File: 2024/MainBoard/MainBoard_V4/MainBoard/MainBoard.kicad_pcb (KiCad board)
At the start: 2 copper layers, 15 parts, among them J1 Raspberry_Pi_2_3, SW1 SW_MEC_5E, U1 STM32F446RETx, Y1 CSTNE16M0V530000R0

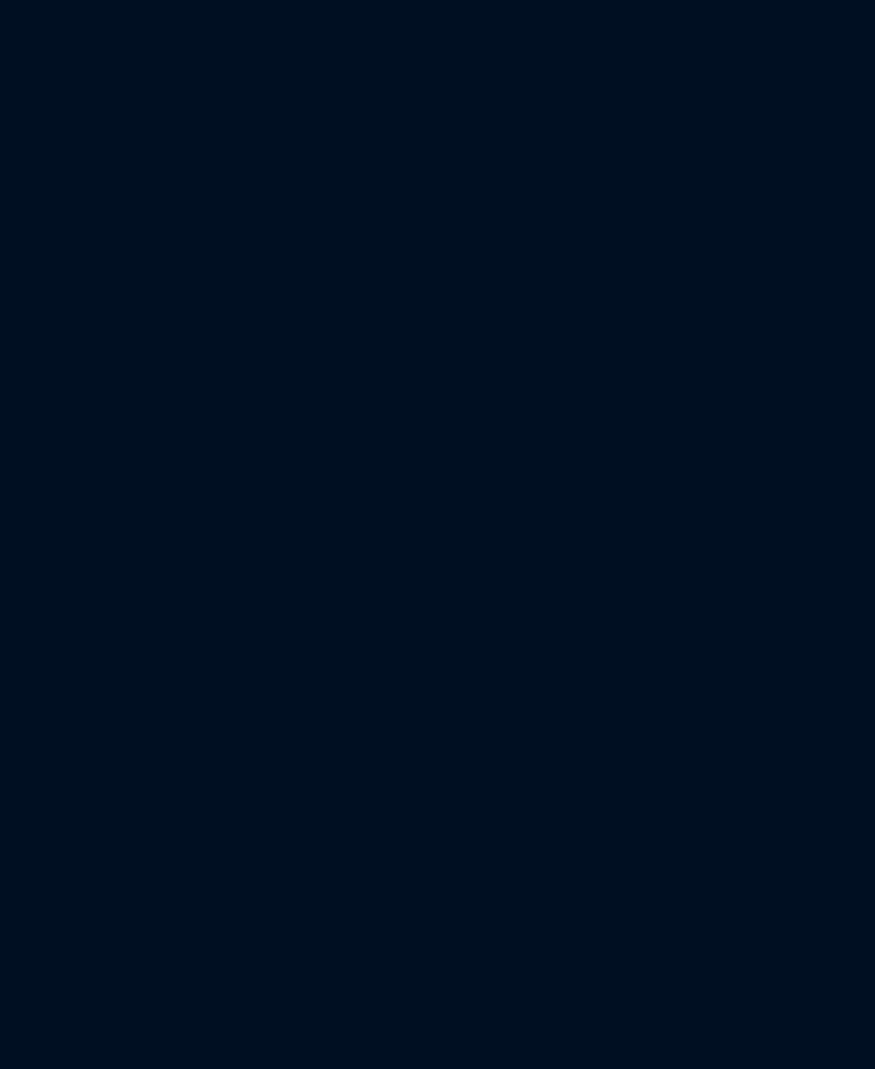
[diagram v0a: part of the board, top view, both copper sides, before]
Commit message: ✨ラズパイ周りとUSBシリアル変換周りの回路図を描いた
 USBを刺した時にラズパイが5Vで起動しないようにしないといけない?
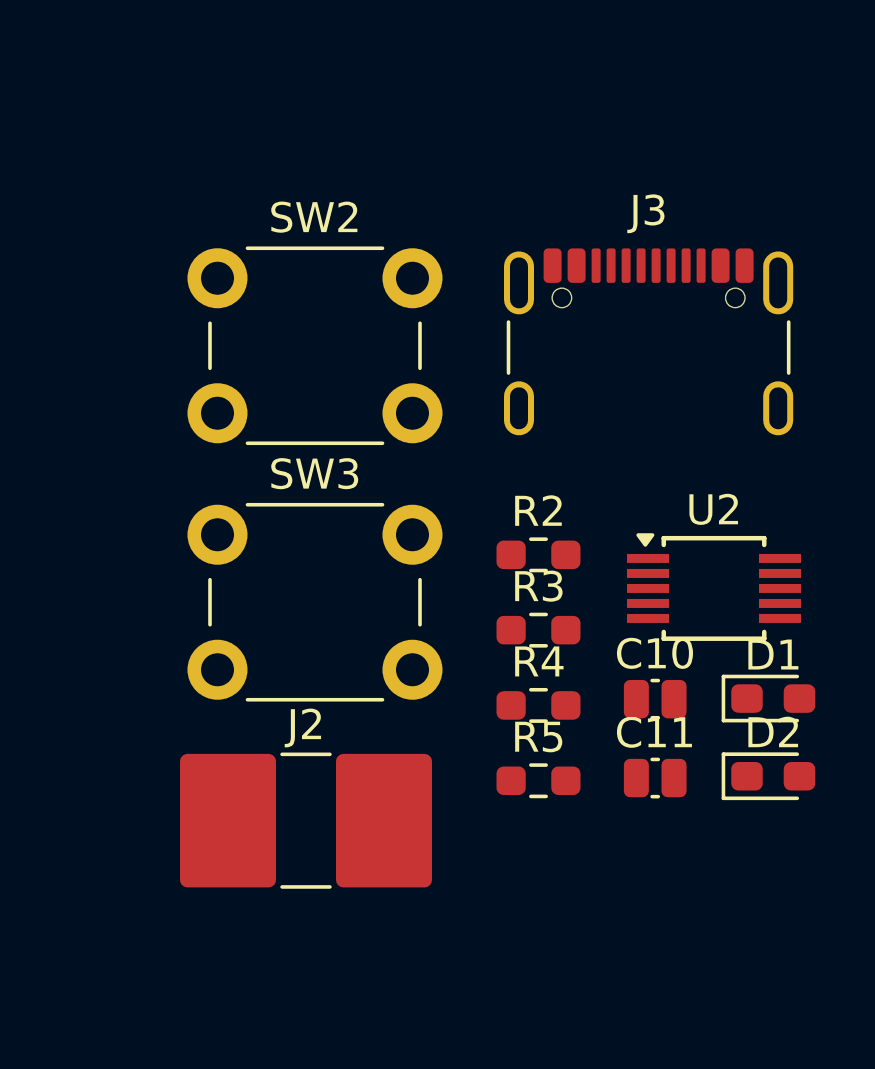
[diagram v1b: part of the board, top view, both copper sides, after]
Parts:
- added C10: 0.1u, Capacitor_SMD:C_0504_1310Metric_Pad0.83x1.28mm_HandSolder, F.Cu at (129.1, 53.7)
- added C11: 0.1u, Capacitor_SMD:C_0504_1310Metric_Pad0.83x1.28mm_HandSolder, F.Cu at (129.1, 56.3)
- added D1: LED, LED_SMD:LED_0603_1608Metric_Pad1.05x0.95mm_HandSolder, F.Cu at (133.0, 53.7)
- added D2: LED, LED_SMD:LED_0603_1608Metric_Pad1.05x0.95mm_HandSolder, F.Cu at (133.0, 56.3)
- added J2: fan, Resistor_SMD:R_2816_7142Metric_Pad3.20x4.45mm_HandSolder, F.Cu at (117.5, 57.8)
- added J3: USB_C_Receptacle_USB2.0_16P, Connector_USB:USB_C_Receptacle_GCT_USB4105-xx-A_16P_TopMnt_Horizontal, F.Cu at (128.9, 42.9)
- added R2: 470, Resistor_SMD:R_0603_1608Metric_Pad0.98x0.95mm_HandSolder, F.Cu at (125.2, 48.9)
- added R3: 5.1k, Resistor_SMD:R_0603_1608Metric_Pad0.98x0.95mm_HandSolder, F.Cu at (125.2, 51.4)
- added R4: 5.1k, Resistor_SMD:R_0603_1608Metric_Pad0.98x0.95mm_HandSolder, F.Cu at (125.2, 53.9)
- added R5: 470, Resistor_SMD:R_0603_1608Metric_Pad0.98x0.95mm_HandSolder, F.Cu at (125.2, 56.4)
- added SW2: SW_MEC_5E, Button_Switch_THT:SW_PUSH_6mm, F.Cu at (114.5, 39.7)
- added SW3: SW_MEC_5E, Button_Switch_THT:SW_PUSH_6mm, F.Cu at (114.5, 48.2)
- added U2: CH340E, Package_SO:MSOP-10_3x3mm_P0.5mm, F.Cu at (131.1, 50.0)
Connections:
- net Net-(J1-5V-Pad2) renamed +5V
- net UART5_TX renamed Ras_RX
- net USB_RX renamed UART2_RX
- net USB_TX renamed UART2_TX
- J1 pad 1: Net-(J1-3V3-Pad1) -> unconnected-(J1-3V3-Pad1)
- J1 pad 10: unconnected-(J1-GPIO15/RXD-Pad10) -> Ras_TX
- J1 pad 12: unconnected-(J1-GPIO18/PWM0-Pad12) -> LED_RAS1
- J1 pad 13: unconnected-(J1-GPIO27-Pad13) -> LED_RAS2
- J1 pad 14: Net-(J1-GND-Pad14) -> GND
- J1 pad 15: unconnected-(J1-GPIO22-Pad15) -> SW_RAS2
- J1 pad 17: Net-(J1-3V3-Pad1) -> unconnected-(J1-3V3-Pad1)
- J1 pad 18: unconnected-(J1-GPIO24-Pad18) -> SW_RAS1
- J1 pad 20: Net-(J1-GND-Pad14) -> GND
- J1 pad 22: unconnected-(J1-GPIO25-Pad22) -> R4
- J1 pad 25: Net-(J1-GND-Pad14) -> GND
- J1 pad 29: unconnected-(J1-GCLK1/GPIO5-Pad29) -> R2
- J1 pad 30: Net-(J1-GND-Pad14) -> GND
- J1 pad 31: unconnected-(J1-GCLK2/GPIO6-Pad31) -> R3
- J1 pad 33: unconnected-(J1-PWM1/GPIO13-Pad33) -> RAS_AUDIO
- J1 pad 34: Net-(J1-GND-Pad14) -> GND
- J1 pad 39: Net-(J1-GND-Pad14) -> GND
- J1 pad 6: Net-(J1-GND-Pad14) -> GND
- J1 pad 7: unconnected-(J1-GCLK0/GPIO4-Pad7) -> R1
- J1 pad 8: unconnected-(J1-GPIO14/TXD-Pad8) -> Ras_TX
- J1 pad 9: Net-(J1-GND-Pad14) -> GND
- U1 pad 42: unconnected-(U1-PA9-Pad42) -> SER_RX
- U1 pad 43: unconnected-(U1-PA10-Pad43) -> SER_TX
- U1 pad 54: UART5_RX -> Ras_TX

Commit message: ✨DXFをインポートした
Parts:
- removed JP1: Jumper_2_Open, Connector_PinHeader_2.54mm:PinHeader_1x02_P2.54mm_Vertical
- added C12: 0.1u, Capacitor_SMD:C_0603_1608Metric_Pad1.08x0.95mm_HandSolder, F.Cu at (82.9, 7.79)
- added C13: 0.1u, Capacitor_SMD:C_0603_1608Metric_Pad1.08x0.95mm_HandSolder, F.Cu at (82.9, 10.3)
- added C14: 1u, Capacitor_SMD:C_0603_1608Metric_Pad1.08x0.95mm_HandSolder, F.Cu at (82.9, 12.8)
- added C15: 1u, Capacitor_SMD:C_0603_1608Metric_Pad1.08x0.95mm_HandSolder, F.Cu at (82.9, 15.3)
- added C16: 0.1u, Capacitor_SMD:C_0603_1608Metric_Pad1.08x0.95mm_HandSolder, F.Cu at (82.9, 17.8)
- added C17: 0.1u, Capacitor_SMD:C_0603_1608Metric_Pad1.08x0.95mm_HandSolder, F.Cu at (82.9, 20.3)
- added C18: 0.1u, Capacitor_SMD:C_0603_1608Metric_Pad1.08x0.95mm_HandSolder, F.Cu at (82.9, 22.8)
- added D10: LED, LED_SMD:LED_0603_1608Metric_Pad1.05x0.95mm_HandSolder, F.Cu at (100.4, 18.2)
- added D11: LED, LED_SMD:LED_0603_1608Metric_Pad1.05x0.95mm_HandSolder, F.Cu at (100.4, 20.8)
- added D12: LED, LED_SMD:LED_0603_1608Metric_Pad1.05x0.95mm_HandSolder, F.Cu at (100.4, 23.4)
- added D13: LED, LED_SMD:LED_0603_1608Metric_Pad1.05x0.95mm_HandSolder, F.Cu at (100.4, 26.0)
- added D14: LED, LED_SMD:LED_0603_1608Metric_Pad1.05x0.95mm_HandSolder, F.Cu at (100.4, 28.5)
- added D15: LED, LED_SMD:LED_0603_1608Metric_Pad1.05x0.95mm_HandSolder, F.Cu at (100.4, 31.1)
- added D3: LED, LED_SMD:LED_0603_1608Metric_Pad1.05x0.95mm_HandSolder, F.Cu at (100.4, 7.83)
- added D4: 1N4148W, Diode_SMD:D_SOD-123, F.Cu at (128.4, 8.21)
- added D5: 1N4148, Diode_THT:D_DO-35_SOD27_P7.62mm_Horizontal, F.Cu at (87.0, 39.4)
- added D6: 1N4148W, Diode_SMD:D_SOD-123, F.Cu at (128.4, 11.6)
- added D7: LED, LED_SMD:LED_0603_1608Metric_Pad1.05x0.95mm_HandSolder, F.Cu at (100.4, 10.4)
- added D8: LED, LED_SMD:LED_0603_1608Metric_Pad1.05x0.95mm_HandSolder, F.Cu at (100.4, 13.0)
- added D9: LED, LED_SMD:LED_0603_1608Metric_Pad1.05x0.95mm_HandSolder, F.Cu at (100.4, 15.6)
- added H1: MountingHole_Pad, MountingHole:MountingHole_3.2mm_M3_Pad_Via, F.Cu at (7.70, -24.2)
- added H2: MountingHole_Pad, MountingHole:MountingHole_3.2mm_M3_Pad_Via, F.Cu at (-50.3, -24.2)
- added H3: MountingHole_Pad, MountingHole:MountingHole_3.2mm_M3_Pad_Via, F.Cu at (44.5, -24.2)
- added H4: MountingHole_Pad, MountingHole:MountingHole_3.2mm_M3_Pad_Via, F.Cu at (-50.3, 24.8)
- added H5: MountingHole_Pad, MountingHole:MountingHole_3.2mm_M3_Pad_Via, F.Cu at (7.70, 24.8)
- added H6: MountingHole_Pad, MountingHole:MountingHole_3.2mm_M3_Pad_Via, F.Cu at (44.5, 24.8)
- added J10: ADC3, Connector_JST:JST_XH_S3B-XH-A_1x03_P2.50mm_Horizontal, F.Cu at (100.2, -3.69)
- added J11: ADC2, Connector_JST:JST_XH_S3B-XH-A_1x03_P2.50mm_Horizontal, F.Cu at (112.1, -3.69)
- added J12: ADC2, Connector_JST:JST_XH_S3B-XH-A_1x03_P2.50mm_Horizontal, F.Cu at (124.1, -3.69)
- added J13: Drib, Connector_JST:JST_XH_S2B-XH-A_1x02_P2.50mm_Horizontal, F.Cu at (88.9, 27.4)
- added J14: UART, Connector_JST:JST_XH_S4B-XH-A_1x04_P2.50mm_Horizontal, F.Cu at (106.0, 9.86)
- added J15: TFT3, Connector_PinHeader_2.54mm:PinHeader_1x04_P2.54mm_Vertical, F.Cu at (125.4, 29.4)
- added J16: CAN_CON, Connector_JST:JST_PH_S2B-PH-K_1x02_P2.00mm_Horizontal, F.Cu at (118.1, 29.4)
- added J4: CAN_CON, Connector_JST:JST_PH_S2B-PH-K_1x02_P2.00mm_Horizontal, F.Cu at (110.2, 29.4)
- added J5: MOLEX MINISPOX, Connector_Molex:Molex_SPOX_5267-06A_1x06_P2.50mm_Vertical, F.Cu at (110.7, 24.2)
- added J6: Debug, Connector_PinHeader_2.54mm:PinHeader_1x07_P2.54mm_Vertical, F.Cu at (83.1, 26.4)
- added J7: ADC0, Connector_JST:JST_XH_S3B-XH-A_1x03_P2.50mm_Horizontal, F.Cu at (64.3, -3.69)
- added J8: ADC1, Connector_JST:JST_XH_S3B-XH-A_1x03_P2.50mm_Horizontal, F.Cu at (76.3, -3.69)
- added J9: ADC2, Connector_JST:JST_XH_S3B-XH-A_1x03_P2.50mm_Horizontal, F.Cu at (88.2, -3.69)
- added Q1: NMOS, MainBoard:SOT95P240X111-3N, F.Cu at (128.4, 15.5)
- added R10: 4.7k, Resistor_SMD:R_0603_1608Metric_Pad0.98x0.95mm_HandSolder, F.Cu at (87.3, 17.8)
- added R11: 1k, Resistor_SMD:R_0603_1608Metric_Pad0.98x0.95mm_HandSolder, F.Cu at (87.3, 20.3)
- added R12: 1k, Resistor_SMD:R_0603_1608Metric_Pad0.98x0.95mm_HandSolder, F.Cu at (87.3, 22.8)
- added R13: 1k, Resistor_SMD:R_0603_1608Metric_Pad0.98x0.95mm_HandSolder, F.Cu at (91.6, 7.79)
- added R14: 1k, Resistor_SMD:R_0603_1608Metric_Pad0.98x0.95mm_HandSolder, F.Cu at (91.6, 10.3)
- added R15: 1k, Resistor_SMD:R_0603_1608Metric_Pad0.98x0.95mm_HandSolder, F.Cu at (91.6, 12.8)
- added R16: 1k, Resistor_SMD:R_0603_1608Metric_Pad0.98x0.95mm_HandSolder, F.Cu at (91.6, 15.3)
- added R17: 1k, Resistor_SMD:R_0603_1608Metric_Pad0.98x0.95mm_HandSolder, F.Cu at (91.6, 17.8)
- added R18: 1k, Resistor_SMD:R_0603_1608Metric_Pad0.98x0.95mm_HandSolder, F.Cu at (91.6, 20.3)
- added R19: 1k, Resistor_SMD:R_0603_1608Metric_Pad0.98x0.95mm_HandSolder, F.Cu at (91.6, 22.8)
- added R20: 120, Resistor_SMD:R_0603_1608Metric_Pad0.98x0.95mm_HandSolder, F.Cu at (96.0, 7.79)
- added R21: 1k, Resistor_SMD:R_0603_1608Metric_Pad0.98x0.95mm_HandSolder, F.Cu at (96.0, 10.3)
- added R22: 1k, Resistor_SMD:R_0603_1608Metric_Pad0.98x0.95mm_HandSolder, F.Cu at (96.0, 12.8)
- added R23: 10K, Resistor_SMD:R_0603_1608Metric_Pad0.98x0.95mm_HandSolder, F.Cu at (96.0, 15.3)
- added R6: 1k, Resistor_SMD:R_0603_1608Metric_Pad0.98x0.95mm_HandSolder, F.Cu at (87.3, 7.79)
- added R7: 1k, Resistor_SMD:R_0603_1608Metric_Pad0.98x0.95mm_HandSolder, F.Cu at (87.3, 10.3)
- added R8: 2.2k, Resistor_SMD:R_0603_1608Metric_Pad0.98x0.95mm_HandSolder, F.Cu at (87.3, 12.8)
- added R9: 2.2k, Resistor_SMD:R_0603_1608Metric_Pad0.98x0.95mm_HandSolder, F.Cu at (87.3, 15.3)
- added SW4: SW_Wuerth_450301014042, Button_Switch_THT:SW_Slide-03_Wuerth-WS-SLTV_10x2.5x6.4_P2.54mm, F.Cu at (71.3, 39.2)
- added U3: MOUDLE-SEEEDUINO-XIAO, MainBoard:MOUDLE14P-SMD-2.54-21X17.8MM, F.Cu at (61.9, 28.1)
- added U4: ~, Connector_PinHeader_2.54mm:PinHeader_1x08_P2.54mm_Vertical, F.Cu at (104.9, 22.4)
- added U5: ~, Connector_PinHeader_2.54mm:PinHeader_1x05_P2.54mm_Vertical, F.Cu at (63.2, 31.2)
- added U6: ~, Connector_PinHeader_2.54mm:PinHeader_1x04_P2.54mm_Vertical, F.Cu at (-3.81, -3.80)
- added U7: AZ1117-3.3, Package_TO_SOT_SMD:SOT-223-3_TabPin2, F.Cu at (70.4, 33.0)
- added U8: MAX3051, Package_SO:SOIC-8_3.9x4.9mm_P1.27mm, F.Cu at (121.2, 9.89)
- C1, C10, C11, C2, C3, C4, C5, C6, C7, C9: footprint Capacitor_SMD:C_0504_1310Metric_Pad0.83x1.28mm_HandSolder -> Capacitor_SMD:C_0603_1608Metric_Pad1.08x0.95mm_HandSolder
- C8: value 0.1u -> 4.7u; footprint Capacitor_SMD:C_0504_1310Metric_Pad0.83x1.28mm_HandSolder -> Capacitor_SMD:C_0603_1608Metric_Pad1.08x0.95mm_HandSolder
- R1: value R -> 10k
- R2: value 470 -> 1k
- moved SW1 148.2 mm to (137.3, -31.0)
- moved C1 148.2 mm to (120.5, -32.1)
- moved C2 148.2 mm to (120.5, -29.4)
- moved C3 148.2 mm to (120.5, -26.8)
- moved C4 148.2 mm to (123.9, -32.1)
- moved C5 148.2 mm to (123.9, -29.4)
- moved C6 148.2 mm to (123.9, -26.8)
- moved C7 148.2 mm to (127.3, -32.1)
- moved C8 148.2 mm to (127.3, -29.4)
- moved C9 148.2 mm to (127.3, -26.8)
- moved R1 148.2 mm to (135.9, -23.9)
- moved U1 148.2 mm to (111.5, -26.2)
- moved Y1 148.2 mm to (136.6, -26.9)
- moved C11 87.1 mm to (86.4, -19.6)
- moved D1 87.1 mm to (90.3, -22.2)
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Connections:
- net Net-(SW1-A) renamed NRST
- net SER_RX renamed UART1_TX
- net SER_TX renamed UART1_RX
- C11 pad 1: +5V -> +5VL
- J3 pad A4: Net-(J3-VBUS-PadA4) -> +5VL
- J3 pad A9: Net-(J3-VBUS-PadA4) -> +5VL
- J3 pad B4: Net-(J3-VBUS-PadA4) -> +5VL
- J3 pad B9: Net-(J3-VBUS-PadA4) -> +5VL
- R2 pad 2: Net-(J3-VBUS-PadA4) -> +5VL
- U1 pad 16: UART2_TX -> Port_RX
- U1 pad 17: UART2_RX -> Port_TX
- U2 pad 10: unconnected-(U2-V3-Pad10) -> Net-(U2-V3)
- U2 pad 7: unconnected-(U2-VCC-Pad7) -> +5VL
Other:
- board outline added: 115.8 x 60 mm

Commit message: 部品をおいた
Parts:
- removed J4: CAN_CON, Connector_JST:JST_PH_S2B-PH-K_1x02_P2.00mm_Horizontal
- added LS1: PKLCS1212E4001-R1, MainBoard:SPKR_PKLCS1212E4001-R1, F.Cu at (27.9, 20.3)
- added ROTSW1: SW_Coded_SH-7070, Button_Switch_THT:Nidec_Copal_SH-7010C, F.Cu at (-60.8, 10.5)
- J10, J11, J12, J7, J8, J9: footprint Connector_JST:JST_XH_S3B-XH-A_1x03_P2.50mm_Horizontal -> Connector_JST:JST_PH_B3B-PH-K_1x03_P2.00mm_Vertical
- J13, J14, J16, J2: moved to B.Cu
- U5: footprint Connector_PinHeader_2.54mm:PinHeader_1x05_P2.54mm_Vertical -> Connector_PinHeader_2.54mm:PinHeader_1x04_P2.54mm_Vertical
- moved J12 186.5 mm to (-60.5, 23.2)
- moved J11 173.6 mm to (-60.4, 16.0)
- moved U4 155.2 mm to (-45.7, -15.2)
- moved J16 151.0 mm to (-32.7, 21.6), turned to 180 degrees
- moved J13 129.1 mm to (-39.9, 18.5), turned to 180 degrees
- moved SW3 129.1 mm to (-55.6, -6.88), turned to -90 degrees
- moved SW2 129.0 mm to (-55.9, -17.8), turned to -90 degrees
- moved J14 125.3 mm to (-19.0, 18.4), turned to 180 degrees
- moved J5 123.2 mm to (-12.5, 25.4)
- moved U8 121.3 mm to (0.00, 12.7)
- moved U5 111.4 mm to (-45.7, 7.62)
- moved J6 106.8 mm to (-22.9, 12.7), turned to 90 degrees
- moved U1 98.4 mm to (17.2, 1.83)
- moved SW1 96.0 mm to (48.3, 5.08), turned to 90 degrees
- moved J15 95.4 mm to (35.6, -2.54)
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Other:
- board size 115.8 x 60 mm -> 115.8 x 60.5 mm

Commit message: わくぎめ
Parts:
- added J4: CAN_CON, Connector_JST:JST_PH_S2B-PH-K_1x02_P2.00mm_Horizontal, F.Cu at (76.3, -6.51)
- J10, J8, J9: footprint Connector_JST:JST_PH_B3B-PH-K_1x03_P2.00mm_Vertical -> Connector_JST:JST_PH_S3B-PH-K_1x03_P2.00mm_Horizontal
- J11, J12, J7: footprint Connector_JST:JST_PH_B3B-PH-K_1x03_P2.00mm_Vertical -> Connector_JST:JST_PH_S3B-PH-K_1x03_P2.00mm_Horizontal; moved to B.Cu
- J5: footprint Connector_Molex:Molex_SPOX_5267-06A_1x06_P2.50mm_Vertical -> Connector_Molex:Molex_SPOX_5268-06A_1x06_P2.50mm_Horizontal; moved to B.Cu
- SW2, SW3: footprint Button_Switch_THT:SW_PUSH_6mm -> MainBoard:SW_SKRPACE010
- moved J7 137.7 mm to (-55.8, 24.6), turned to 90 degrees
- moved C1 64.4 mm to (58.1, -16.2)
- moved C2 64.4 mm to (58.1, -13.6)
- moved C3 64.4 mm to (58.1, -10.9)
- moved C4 64.4 mm to (61.5, -16.2)
- moved C5 64.4 mm to (61.5, -13.6)
- moved C6 64.4 mm to (61.5, -10.9)
- moved C7 64.4 mm to (64.9, -16.2)
- moved C8 64.4 mm to (64.9, -13.6)
- moved C9 64.4 mm to (64.9, -10.9)
- moved U7 57.2 mm to (15.6, 16.5)
- moved SW2 27.4 mm to (-60.4, 9.23)
- moved J16 15.9 mm to (-16.8, 21.3)
- moved J5 14.4 mm to (1.23, 21.1), turned to 180 degrees
- moved ROTSW1 12.5 mm to (-61.0, -1.95)
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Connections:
- J1 pad 10: Ras_TX -> Ras_RX

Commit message: 途中経過
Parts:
- added Q2: PMOS, Package_TO_SOT_SMD:SOT-23, F.Cu at (14.3, 22.0)
- added Q3: PMOS, Package_TO_SOT_SMD:SOT-23, F.Cu at (18.5, 22.0)
- D5: footprint Diode_THT:D_DO-35_SOD27_P7.62mm_Horizontal -> Diode_SMD:D_SOD-123
- moved C10 134.8 mm to (-48.1, -30.2)
- moved D6 128.4 mm to (0.76, 26.2), turned to 180 degrees
- moved Y1 126.5 mm to (13.2, 0.91), turned to -90 degrees
- moved Q1 98.6 mm to (30.4, 26.3)
- moved R10 94.5 mm to (-6.84, 26.2)
- moved R11 90.9 mm to (-3.41, 26.2)
- moved R9 86.4 mm to (2.54, -1.52)
- moved R8 86.2 mm to (2.54, -3.17)
- moved D15 86.1 mm to (130.5, -49.5)
- moved R22 83.0 mm to (14.1, 26.3), turned to 180 degrees
- moved R23 76.4 mm to (20.3, 26.2), turned to 180 degrees
- moved D10 72.1 mm to (113.6, -52.7)
- moved D11 72.1 mm to (113.6, -50.1)
- moved D12 72.1 mm to (113.6, -47.5)
- moved D13 72.1 mm to (113.6, -44.9)
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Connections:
- J16 pad 1: CANH -> CANL
- J16 pad 2: CANL -> CANH
- J6 pad 1: UART_RX -> UART1_TX
- J6 pad 2: UART_TX -> UART1_RX
- J6 pad 6: VDD -> +3.3V
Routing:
- net GND: track 0.00 -> 243.3 mm, vias 0 -> 3
- net +3.3V: track 0.00 -> 237.3 mm
- net +5V: track 0.00 -> 160.2 mm, vias 0 -> 1
- net MOSI: track 0.00 -> 114.4 mm, vias 0 -> 2
- net MISO: track 0.00 -> 109.9 mm, vias 0 -> 2
- net SCK: track 0.00 -> 108.8 mm, vias 0 -> 2
- net LED_CS: track 0.00 -> 104.0 mm
- net T_CS: track 0.00 -> 85.8 mm
- net Ras_TX: track 0.00 -> 84.4 mm, vias 0 -> 1
- net LCD_LED: track 0.00 -> 81.8 mm, vias 0 -> 1
- net Ras_RX: track 0.00 -> 81.8 mm, vias 0 -> 1
- net D/C: track 0.00 -> 79.5 mm
- net Reset: track 0.00 -> 78.4 mm
- net +5VL: track 0.00 -> 64.2 mm, vias 0 -> 4
- net SWCLK: track 0.00 -> 54.3 mm, vias 0 -> 2
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
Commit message: 8割完成
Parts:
- removed J10: ADC3, Connector_JST:JST_PH_S3B-PH-K_1x03_P2.00mm_Horizontal
- removed J4: CAN_CON, Connector_JST:JST_PH_S2B-PH-K_1x02_P2.00mm_Horizontal
- removed J8: ADC1, Connector_JST:JST_PH_S3B-PH-K_1x03_P2.00mm_Horizontal
- removed J9: ADC2, Connector_JST:JST_PH_S3B-PH-K_1x03_P2.00mm_Horizontal
- R8, R9: moved to B.Cu
- moved R1 99.4 mm to (39.7, 1.40), turned to 90 degrees
- moved R20 92.5 mm to (-5.40, 16.4), turned to 180 degrees
- moved C16 76.7 mm to (6.30, 15.6), turned to -90 degrees
- moved D4 57.5 mm to (75.2, 30.2)
- moved D6 24.4 mm to (8.40, 3.00), turned to -90 degrees
- moved R11 22.4 mm to (8.40, 7.17), turned to 90 degrees
- moved R5 22.0 mm to (84.4, -41.5)
- moved D2 22.0 mm to (92.2, -41.6)
- moved D1 22.0 mm to (92.2, -44.2)
- moved R2 22.0 mm to (84.4, -49.0)
- moved R10 21.8 mm to (8.40, 10.6), turned to 90 degrees
- moved C9 19.4 mm to (49.8, 1.20), turned to 180 degrees
- moved C8 18.5 mm to (11.7, 11.2)
- moved D5 17.7 mm to (75.0, 26.4)
- moved C5 17.5 mm to (14.1, -2.96), turned to -90 degrees
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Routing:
- net GND: track 243.3 -> 443.7 mm, vias 3 -> 8
- net NRST: track 0.00 -> 93.7 mm, vias 0 -> 3
- net ADC_PHOTO1: track 0.00 -> 93.2 mm, vias 0 -> 4
- net ADC_SUB0: track 0.00 -> 89.5 mm, vias 0 -> 3
- net ADC_PHOTO0: track 0.00 -> 84.2 mm, vias 0 -> 3
- net +5V: track 160.2 -> 234.5 mm, vias 1 -> 3
- net DRIB_OUT: track 0.00 -> 72.7 mm, vias 0 -> 3
- net Port_RX: track 0.00 -> 65.9 mm, vias 0 -> 2
- net +3.3V: track 237.3 -> 302.7 mm
- net Port_TX: track 0.00 -> 63.7 mm, vias 0 -> 2
- net UART1_TX: track 25.6 -> 85.7 mm, vias 2 -> 4
- net UART1_RX: track 26.3 -> 81.2 mm, vias 2 -> 3
- net I2C_SDA: track 23.1 -> 30.5 mm, vias 1 -> 4
- net SWDIO: track 50.3 -> 57.7 mm
- net UART4_RX: track 22.0 -> 29.2 mm
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- added copper zone on B.Cu, net GND
- added copper zone on F.Cu, net GND

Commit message: レビュー前
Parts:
- removed D12, D15: LED, LED_SMD:LED_0603_1608Metric_Pad1.05x0.95mm_HandSolder
- removed R17, R21: 1k, Resistor_SMD:R_0603_1608Metric_Pad0.98x0.95mm_HandSolder
- removed SW2, SW3: SW_MEC_5E, MainBoard:SW_SKRPACE010
- added SW5: Ras_1, Button_Switch_THT:SW_PUSH_6mm_H7.3mm, F.Cu at (-60.4, -23.1)
- added SW6: Ras_2, Button_Switch_THT:SW_PUSH_6mm_H7.3mm, F.Cu at (-60.4, -13.3)
- C10: moved to B.Cu
- moved D14 181.7 mm to (-61.0, 8.07), turned to 90 degrees
- moved D13 180.9 mm to (-59.4, 8.07), turned to 90 degrees
- moved R19 174.4 mm to (-61.0, 4.64), turned to -90 degrees
- moved R18 173.6 mm to (-59.4, 4.65), turned to -90 degrees
- moved D3 89.6 mm to (47.8, -17.3), turned to 90 degrees
- moved D7 88.2 mm to (43.6, -6.62), turned to -90 degrees
- moved R6 85.1 mm to (47.8, -13.8), turned to -90 degrees
- moved D10 82.4 mm to (45.2, -6.62), turned to -90 degrees
- moved D8 80.9 mm to (43.6, -17.3), turned to 90 degrees
- moved D4 79.3 mm to (8.80, -13.2), turned to 90 degrees
- moved D5 79.3 mm to (6.30, -13.2), turned to 90 degrees
- moved D9 78.2 mm to (45.2, -17.3), turned to 90 degrees
- moved R13 77.5 mm to (43.6, -13.8), turned to -90 degrees
- moved R15 75.3 mm to (45.2, -10.2), turned to 90 degrees
- moved R14 74.7 mm to (45.2, -13.8), turned to -90 degrees
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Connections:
- D1 pad 1: GND -> Net-(D1-K)
- D1 pad 2: Net-(D1-A) -> +5VL
- D10 pad 1: GND -> Net-(D10-K)
- D10 pad 2: Net-(D10-A) -> HEART_BEAT_LED
- D11 pad 1: GND -> Net-(D11-K)
- D11 pad 2: Net-(D11-A) -> +3.3V
- D2 pad 1: GND -> Net-(D2-K)
- D3 pad 1: GND -> Net-(D3-K)
- D3 pad 2: Net-(D3-A) -> +5V
- D7 pad 1: GND -> Net-(D7-K)
- D7 pad 2: Net-(D7-A) -> LED0
- D8 pad 1: GND -> Net-(D8-K)
- D8 pad 2: Net-(D8-A) -> LED1
- D9 pad 1: GND -> Net-(D9-K)
- D9 pad 2: Net-(D9-A) -> LED2
- H1 pad 1: GND -> unconnected-(H1-Pad1)
- H2 pad 1: GND -> unconnected-(H2-Pad1)
- H3 pad 1: GND -> unconnected-(H3-Pad1)
- H4 pad 1: GND -> unconnected-(H4-Pad1)
- H5 pad 1: GND -> unconnected-(H5-Pad1)
- H6 pad 1: GND -> unconnected-(H6-Pad1)
- R12 pad 1: LED0 -> Net-(D7-K)
- R12 pad 2: Net-(D7-A) -> GND
- R13 pad 1: LED1 -> Net-(D8-K)
- R13 pad 2: Net-(D8-A) -> GND
- R14 pad 1: LED2 -> Net-(D9-K)
- R14 pad 2: Net-(D9-A) -> GND
- R15 pad 1: LED3 -> Net-(D10-K)
- R15 pad 2: Net-(D10-A) -> GND
- R16 pad 1: LED4 -> Net-(D11-K)
- R16 pad 2: Net-(D11-A) -> GND
- R2 pad 1: Net-(D1-A) -> GND
- R2 pad 2: +5VL -> Net-(D1-K)
- R5 pad 1: Net-(D2-A) -> Net-(D2-K)
- R5 pad 2: Net-(U2-TNOW) -> GND
- R6 pad 1: +5V -> Net-(D3-K)
- R6 pad 2: Net-(D3-A) -> GND
- U2 pad 6: Net-(U2-TNOW) -> Net-(D2-A)
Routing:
- net GND: track 443.7 -> 637.3 mm, vias 8 -> 116
- net Net-(D4-K): track 0.00 -> 64.4 mm, vias 0 -> 2
- net R2: track 0.00 -> 62.3 mm, vias 0 -> 1
- net R3: track 0.00 -> 61.8 mm, vias 0 -> 1
- net R4: track 0.00 -> 53.7 mm, vias 0 -> 1
- net LED_RAS2: track 0.00 -> 47.7 mm, vias 0 -> 1
- net LED0: track 0.00 -> 46.4 mm, vias 0 -> 4
- net LED_RAS1: track 0.00 -> 46.2 mm, vias 0 -> 1
- net SW_RAS2: track 0.00 -> 45.0 mm, vias 0 -> 1
- net LED2: track 0.00 -> 42.4 mm, vias 0 -> 4
- net HEART_BEAT_LED: track 0.00 -> 42.1 mm, vias 0 -> 4
- net LED1: track 0.00 -> 41.2 mm, vias 0 -> 4
- net SW_RAS1: track 0.00 -> 39.1 mm, vias 0 -> 1
- net R1: track 0.00 -> 37.7 mm, vias 0 -> 1
- net +3.3V: track 302.7 -> 340.0 mm, vias 0 -> 2
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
